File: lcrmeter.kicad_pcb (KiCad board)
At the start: 2 copper layers, 71.9 x 54.1 mm, 63 parts, among them J1 LCR_input, J2 LCR_input, J3 Conn_01x06, J4 USB_B_Micro, J5 OSCILLOSCOPE, J6 misc, J7 misc, SW1 power, SW2 +, SW3 -, SW4 ok, SW5 back, U1 MCP47, U2 STM32F103C8Tx, U3 OLED, U4 74HC14, U5 MCP6001-OT, Y1 8Mhz

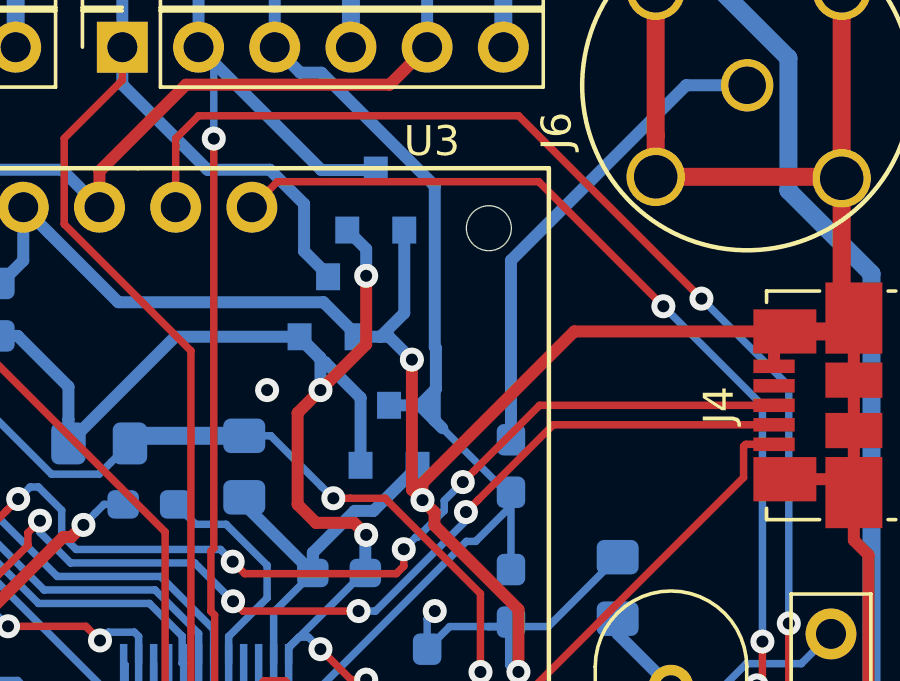
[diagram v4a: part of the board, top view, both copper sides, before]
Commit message: fix oscilloscope connection
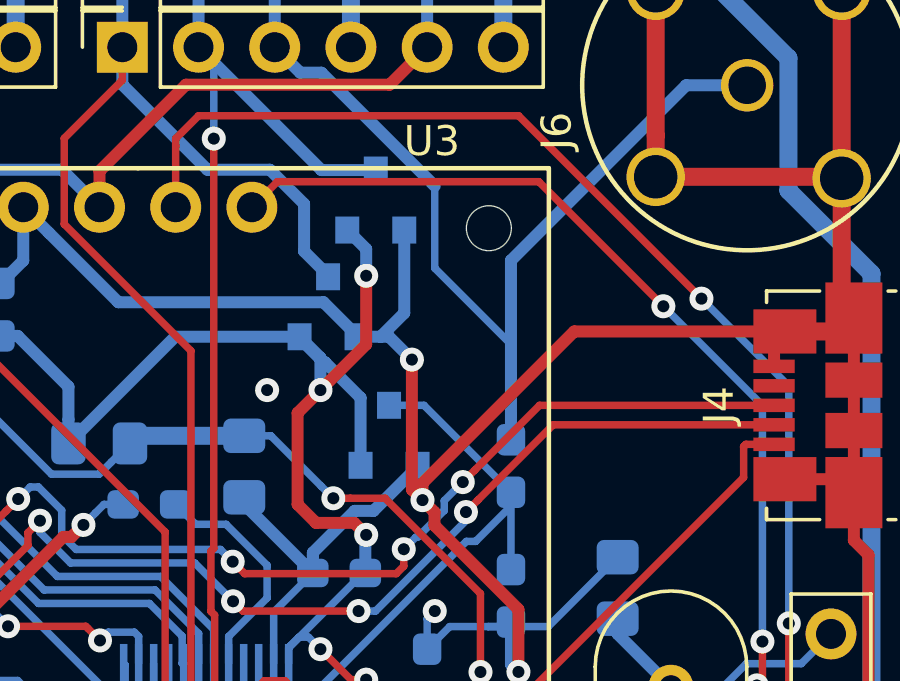
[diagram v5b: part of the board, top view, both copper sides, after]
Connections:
- J5 pad 1: Net-(J5-Pad1) -> /OSCILLOSCOPE_IN
- J6 pad 3: /OSCILLOSCOPE -> /OSCILLOSCOPE_IN
- J7 pad 3: /OSCILLOSCOPE -> /OSCILLOSCOPE_IN
- R17 pad 1: Net-(J5-Pad1) -> /OSCILLOSCOPE_IN
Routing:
- net /OSCILLOSCOPE_IN: track 0.00 -> 33.3 mm
- net /OSCILLOSCOPE: track 44.6 -> 25.9 mm
- net Net-(J5-Pad1): track 16.1 -> 0.00 mm
